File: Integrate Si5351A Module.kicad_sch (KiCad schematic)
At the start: 0 parts

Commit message: Added Footprints folder
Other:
- added sheet Input Power Stage (Input_Power_Stage.kicad_sch)
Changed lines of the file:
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@@
 	(generator_version "9.0")
 	(paper "A4")
+	(sheet
+		(at 19.17 19.38)
+		(size 20 12)
+		(exclude_from_sim no)
+		(in_bom yes)
+		(on_board yes)
+		(dnp no)
+		(fields_autoplaced yes)
+		(stroke
+			(width 0.1524)
+			(type solid)
+		)
+		(fill
+			(color 0 0 0 0.0000)
+		)
+		(property "Sheetname" "Input Power Stage"
+			(at 19.17 18.6684 0)
+			(effects
+				(font
+					(size 1.27 1.27)
+				)
+				(justify left bottom)
+			)
+		)
+		(property "Sheetfile" "Input_Power_Stage.kicad_sch"
+			(at 19.17 31.9646 0)
+			(effects
+				(font
+					(size 1.27 1.27)
+				)
+				(justify left top)
+			)
+		)
+		(instances
+			(project "Integrate Si5351A Module"
+				(path "/5effc93d-4636-458a-a65b-e63d3c617be7"
+					(page "2")
+				)
+			)
+		)
+	)
 	(sheet_instances
 		(path "/"

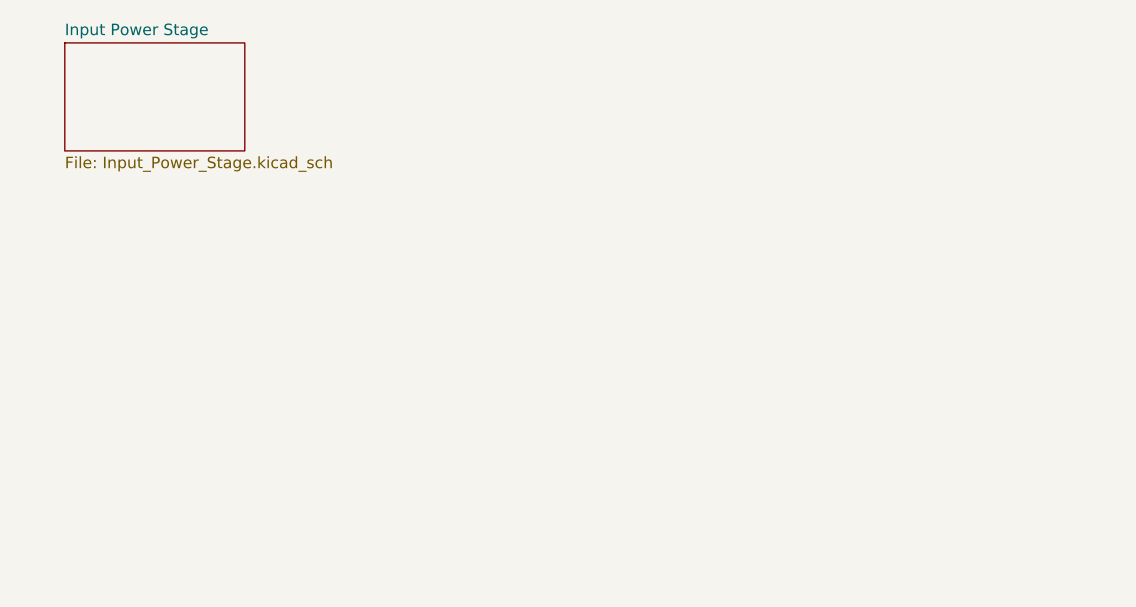
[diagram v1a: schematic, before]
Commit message: - Renamed USB-C connector folder - Finished USB-C connector schematic
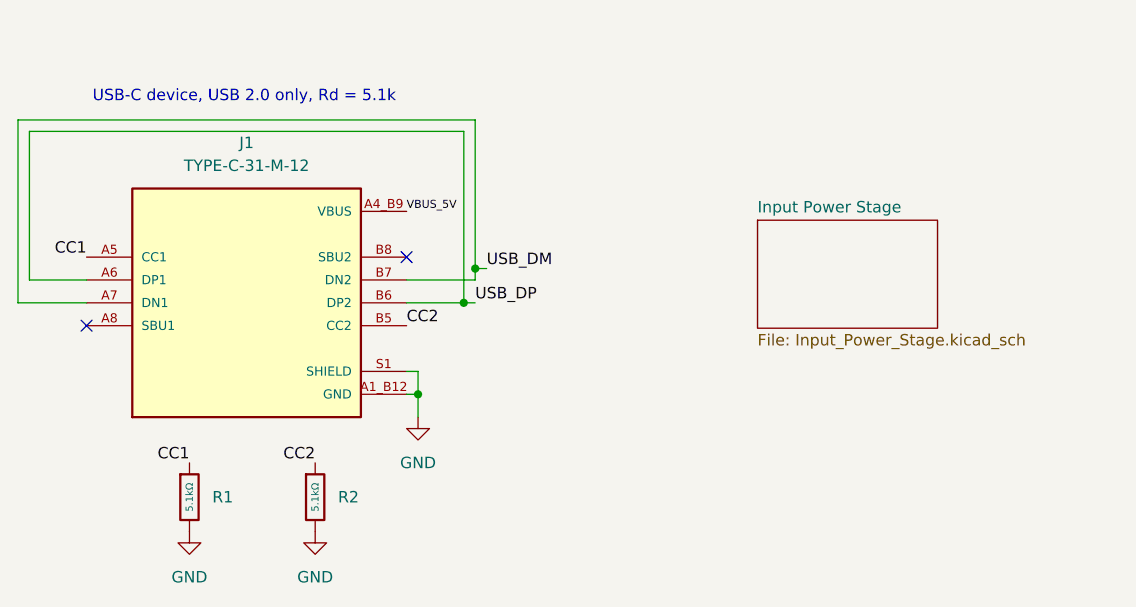
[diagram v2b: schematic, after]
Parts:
- added J1: TYPE-C-31-M-12, TYPE-C-31-M-12:HRO_TYPE-C-31-M-12, symbol TYPE-C-31-M-12:TYPE-C-31-M-12
- added R1, R2: 5.1kΩ, PCM_JLCPCB:R_0603, symbol PCM_JLCPCB-Resistors:0603,5.1kΩ
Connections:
- new net CC1: J1.A5 (CC1), R1.1
- new net CC2: J1.B5 (CC2), R2.1
- new net GND: J1.A1_B12 (GND), J1.B1_A12 (GND), J1.S1 (SHIELD), J1.S2 (SHIELD), J1.S3 (SHIELD), J1.S4 (SHIELD), R1.2, R2.2
- new net USB_DM: J1.A7 (DN1), J1.B7 (DN2)
- new net USB_DP: J1.A6 (DP1), J1.B6 (DP2)
- new net VBUS: J1.A4_B9 (VBUS), J1.B4_A9 (VBUS)
- no-connect marks 0 -> 2
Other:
- note added: "USB-C device, USB 2.0 only, Rd = 5.1k"

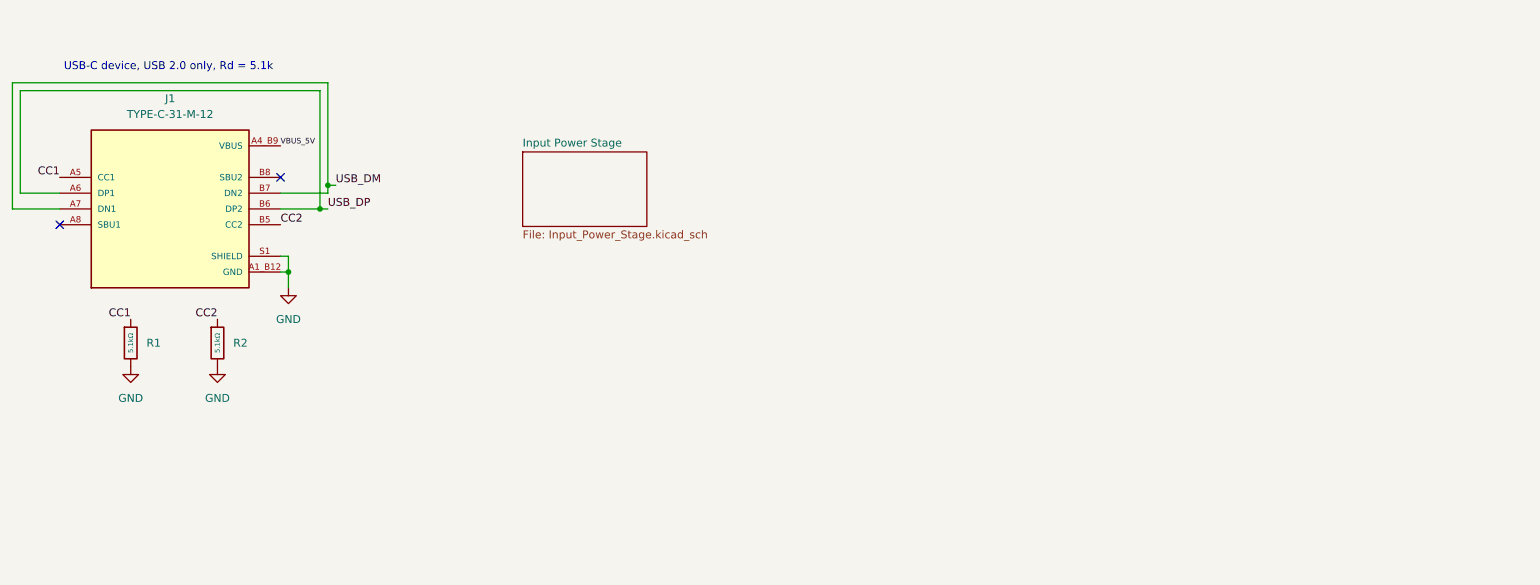
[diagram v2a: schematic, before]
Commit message: Finished 5V_Barrel over voltage red LED indicator
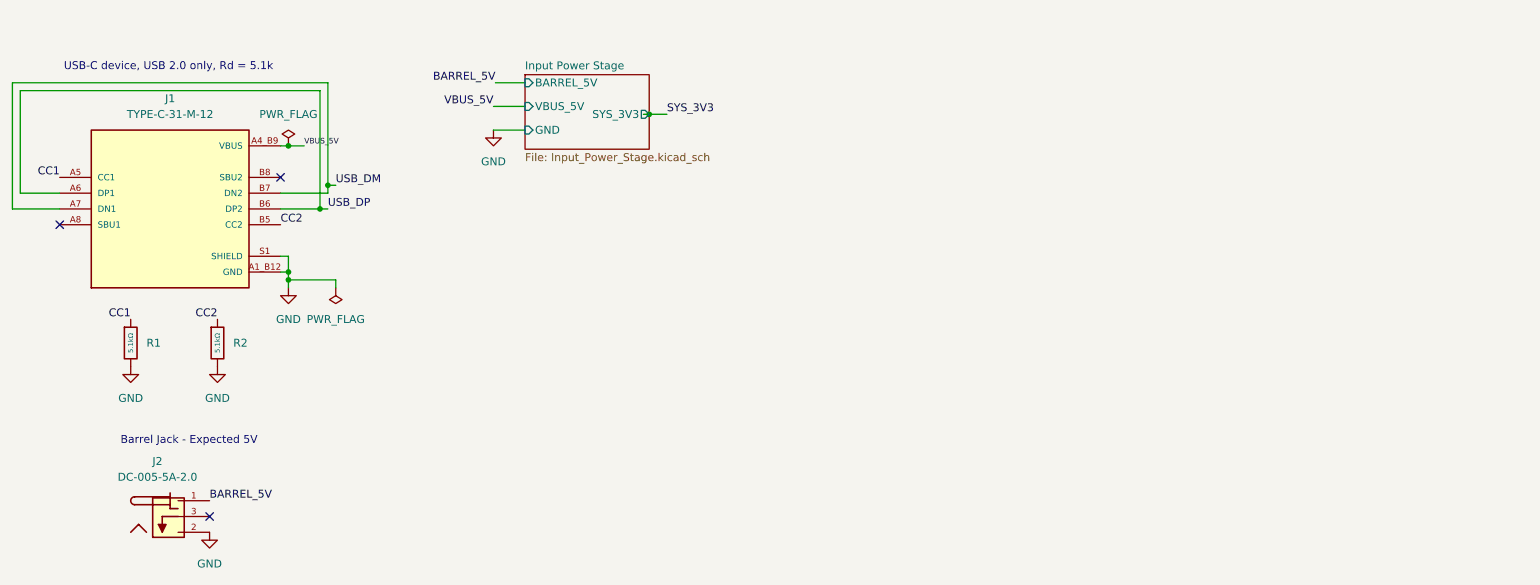
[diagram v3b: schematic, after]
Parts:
- added J2: DC-005-5A-2.0, DC-005-5A-2.0:XKB_DC-005-5A-2.0, symbol DC-005-5A-2.0:DC-005-5A-2.0
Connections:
- net GND: now also J2.2
- new net BARREL_5V: J2.1
- no-connect marks 2 -> 3
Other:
- sheet Input Power Stage ports: added BARREL_5V, GND, SYS_3V3, VBUS_5V; removed none
- note added: "Barrel Jack - Expected 5V"
- company: (none) -> Yaniv Lieberman
- title: (none) -> Integrated Si5351A Module

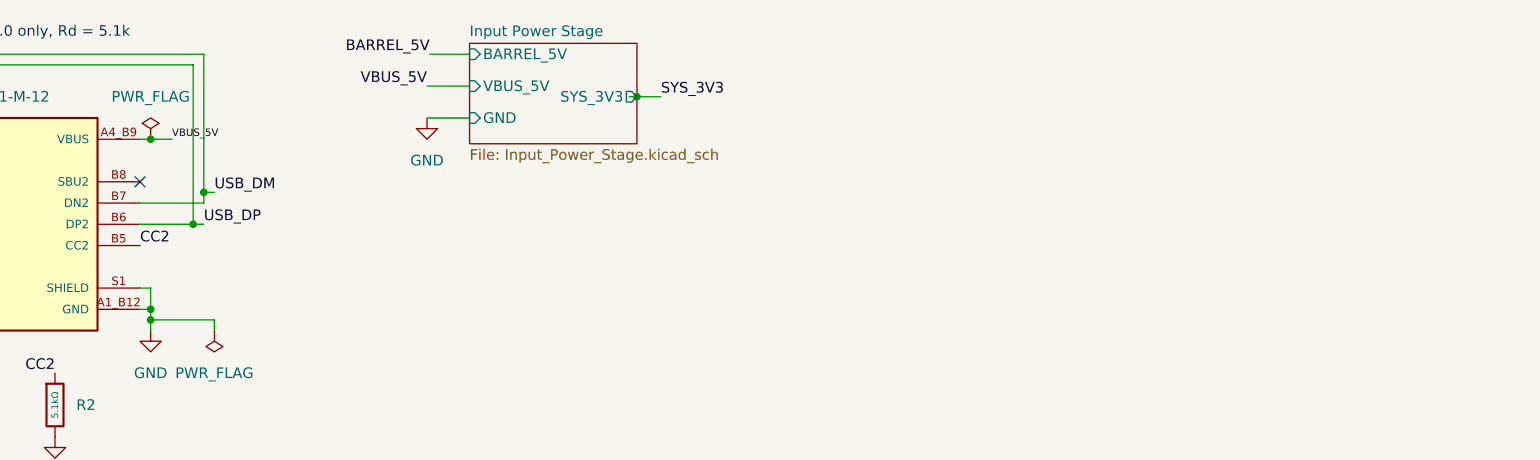
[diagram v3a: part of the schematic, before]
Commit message: Finished USB programming stage
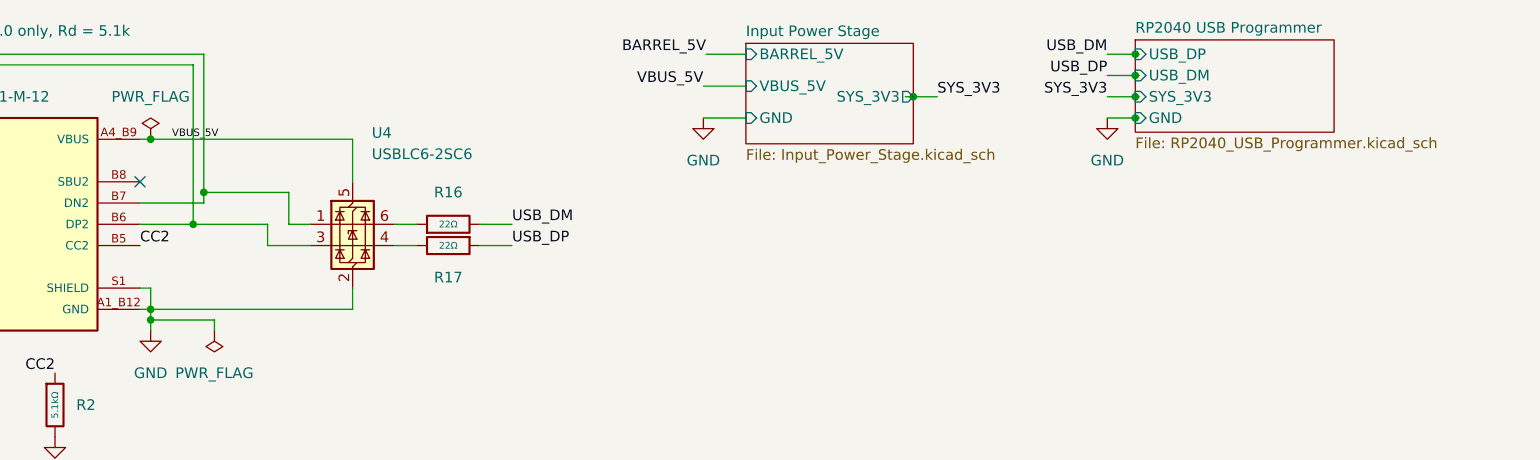
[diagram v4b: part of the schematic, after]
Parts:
- added R16, R17: 22Ω, PCM_JLCPCB:R_0603, symbol PCM_JLCPCB-Resistors:0603,22Ω
- added U4: USBLC6-2SC6, Package_TO_SOT_SMD:SOT-23-6, symbol Power_Protection:USBLC6-2SC6
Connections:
- net GND: now also U4.2 (GND)
- net USB_DM: now also R16.2; no longer J1.A7 (DN1), J1.B7 (DN2)
- net USB_DP: now also R17.1; no longer J1.A6 (DP1), J1.B6 (DP2)
- net VBUS: now also U4.5 (VBUS)
- new net: J1.A6 (DP1), J1.B6 (DP2), U4.3 (I/O2)
- new net: J1.A7 (DN1), J1.B7 (DN2), U4.1 (I/O1)
- new net: R17.2, U4.4 (I/O2)
- new net: R16.1, U4.6 (I/O1)
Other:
- added sheet RP2040 USB Programmer (RP2040_USB_Programmer.kicad_sch)

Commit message: Finished STM32 Stage
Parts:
- renumbered J2 to J1, J1 to J2, R16 to R3, R17 to R4, U4 to U1
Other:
- added sheet STM32 MCU Stage (untitled.kicad_sch)
- sheet RP2040 USB Programmer ports: added NRST_TARGET, SWCLK, SWDIO, SWO, UART_DBG_RX, UART_DBG_TX; removed none
